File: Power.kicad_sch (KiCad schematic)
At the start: 41 parts, among them IC1 TPS65251-1RHAR

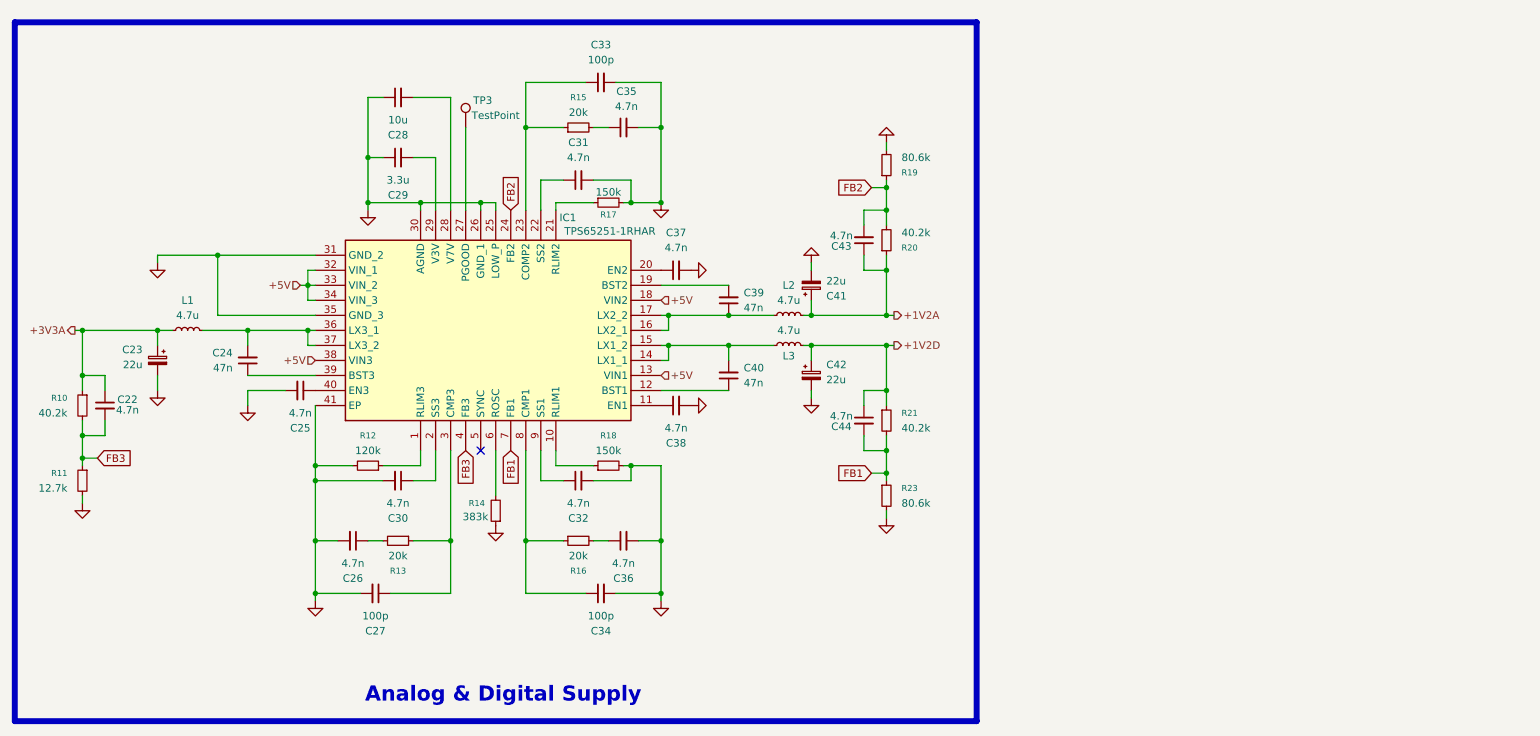
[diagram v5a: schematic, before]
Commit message: Removed Ethernet
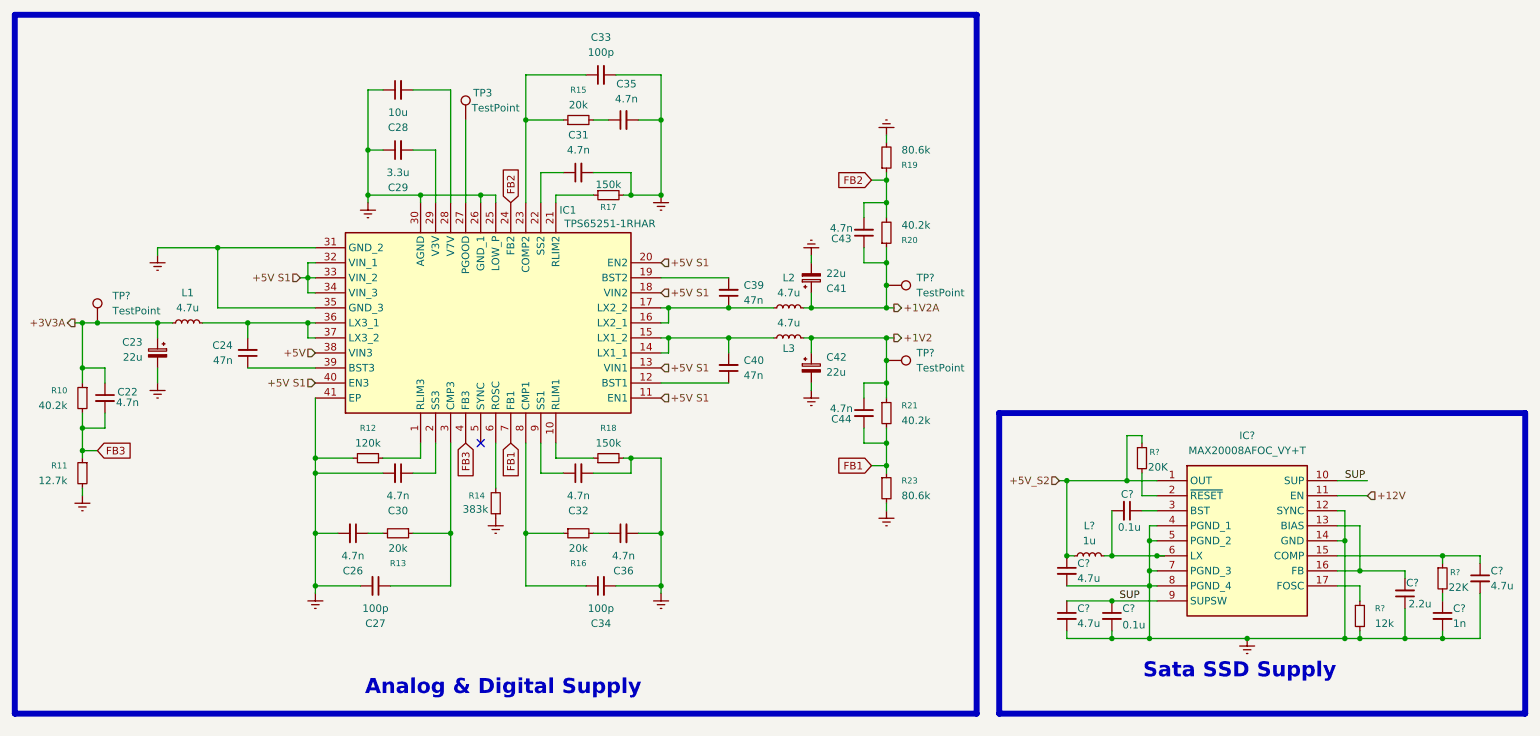
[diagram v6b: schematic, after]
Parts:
- removed C25, C37, C38: 4.7n, symbol Device:C_Small
- added C? (x2): 0.1u, symbol Device:C_Small
- added C? (x3): 4.7u, symbol Device:C_Small
- added C?: 2.2u, symbol Device:C_Small
- added C?: 1n, symbol Device:C_Small
- added IC?: MAX20008AFOC_VY+T, MAX20008AFOCVYT, symbol MAX20008AFOC_VY+T:MAX20008AFOC_VY+T
- added L?: 1u, symbol Device:L_Small
- added R?: 12k, symbol Device:R_Small
- added R?: 22K, symbol Device:R_Small
- added R?: 20K, symbol Device:R_Small
- added TP? (x3): TestPoint, symbol Connector:TestPoint
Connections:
- net +1V2A: now also TP?.1
- net +3V3A: now also TP?.1
- net +5V: no longer IC1.13 (VIN1), IC1.18 (VIN2), IC1.32 (VIN_1), IC1.33 (VIN_2), IC1.34 (VIN_3)
- net +5V S1: now reaches IC1.40 (EN3)
- net +5V S1: now also IC1.11 (EN1), IC1.13 (VIN1), IC1.18 (VIN2), IC1.20 (EN2), IC1.32 (VIN_1), IC1.33 (VIN_2), IC1.34 (VIN_3)
- net +1V2D renamed +1V2
- net +1V2: now also TP?.1
- new net: C?.1, C?.2, C?.2, C?.2, C?.2, C?.2, IC?.12 (SYNC), IC?.14 (GND), IC?.4 (PGND_1), IC?.5 (PGND_2), IC?.7 (PGND_3), IC?.8 (PGND_4), R?.2
- new net: C?.2, IC?.13 (BIAS), IC?.16 (FB)
- new net: C?.1, IC?.15 (COMP), R?.1
- new net: IC?.17 (FOSC), R?.1
- new net: IC?.2 (~{RESET}), R?.2
- new net: C?.1, IC?.3 (BST)
- new net: C?.2, IC?.6 (LX), L?.1
- new net: C?.1, R?.2
- new net +12V: IC?.11 (EN)
- new net +5V_S2: C?.1, IC?.1 (OUT), L?.2, R?.1
- new net SUP: C?.1, C?.1, IC?.10 (SUP), IC?.9 (SUPSW)
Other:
- moved on the sheet: C22, C23, C24, C26, C27, C28, C29, C30, C31, C32, C33, C34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
